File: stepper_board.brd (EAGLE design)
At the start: 100 x 80 mm, 77 parts, among them IC1 MCP1703DB, U2 MIC2005A-1YM5, Y1 12 MHz

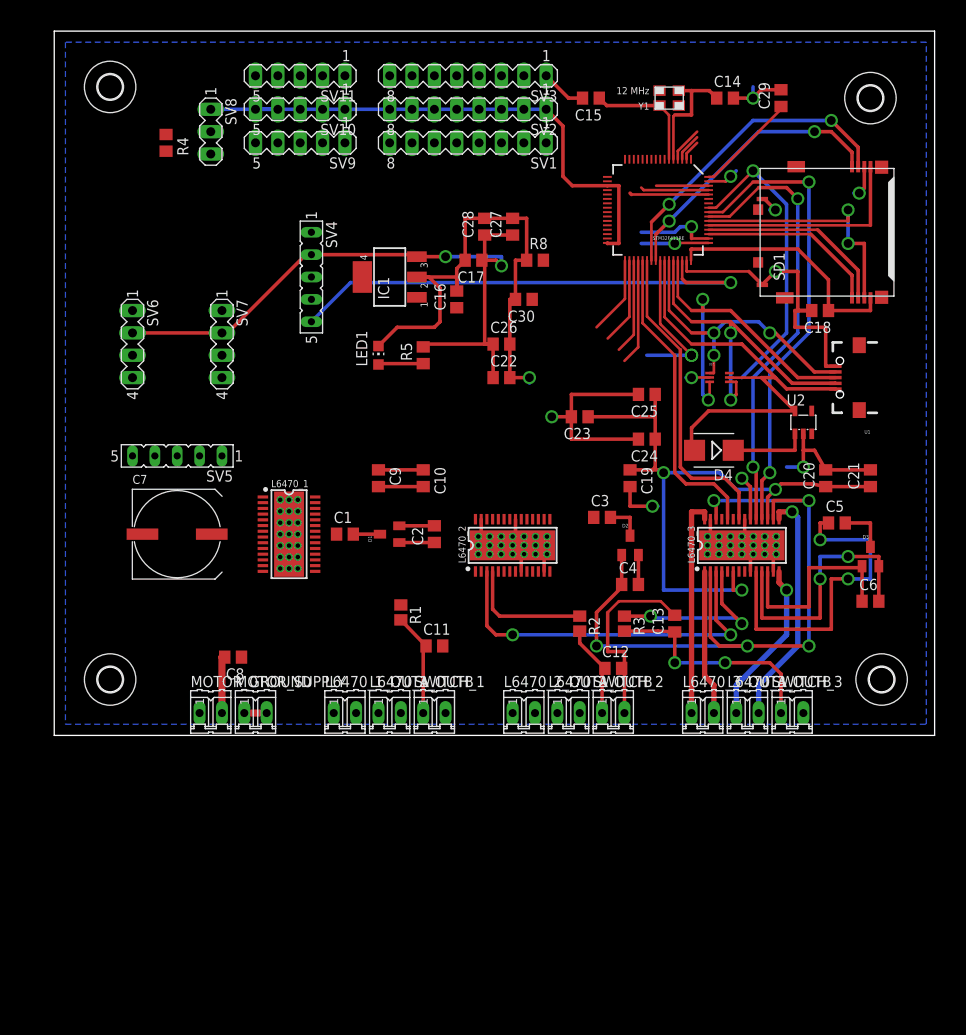
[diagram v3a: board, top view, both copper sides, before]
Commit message: Changed L6470 package footprint, added chip select pins to drivers, started routing
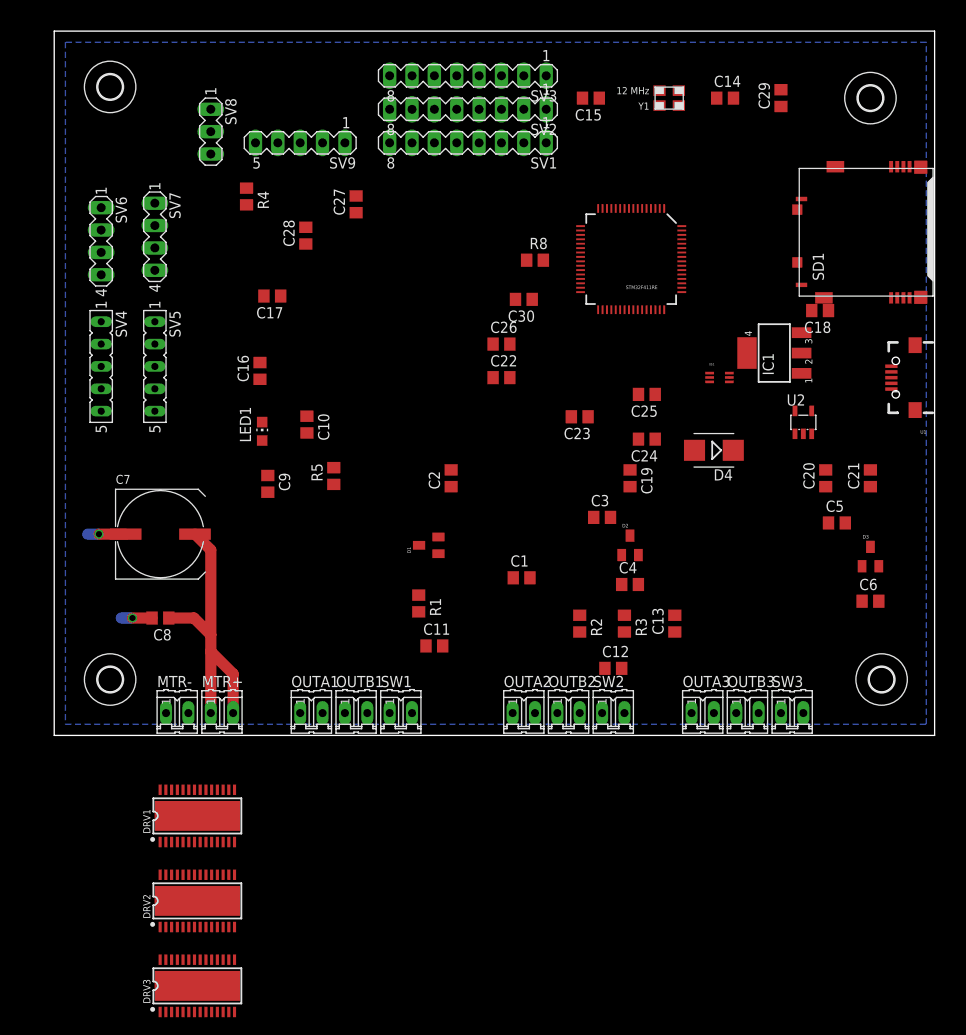
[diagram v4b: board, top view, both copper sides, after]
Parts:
- removed L6470_1, L6470_2, L6470_3: (no value), SparkFun-PowerIC:HTSSOP28
- removed L6470_1_OUTA, L6470_1_OUTB, MOTOR_GROUND, MOTOR_SUPPLY, SWITCH_1: (no value), con-amp-quick:02P
- removed SV10, SV11: (no value), con-lstb:MA05-1
- added DRV1, DRV2, DRV3: (no value), PowerIC_spark:HTSSOP28-NOPAD
- added MTR+, MTR-, OUTA1, OUTB1, SW1: (no value), con-amp-quick:02P
- moved IC1 44.5 mm to (81.8, 43.4)
- moved SV4 25.9 mm to (5.33, 41.9)
- moved C16 23.8 mm to (23.4, 41.4)
- moved C17 23.2 mm to (24.8, 49.9)
- moved C1 20.7 mm to (53.1, 17.9)
- moved C28 20.3 mm to (28.6, 56.8)
- moved C27 18.0 mm to (34.3, 60.3)
- moved R5 17.1 mm to (31.8, 29.5)
- moved LED1 15.8 mm to (23.6, 34.5)
- moved C10 14.5 mm to (28.7, 35.3)
- moved SV7 14.4 mm to (11.4, 56.6)
- moved C9 12.6 mm to (24.3, 28.6)
- moved SV6 12.2 mm to (5.33, 56.1)
- moved R4 11.0 mm to (21.8, 61.2)
- moved SV5 10.5 mm to (11.4, 41.9), turned to 270 degrees
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- renumbered L6470_2_OUTA to OUTA2, L6470_2_OUTB to OUTB2, L6470_3_OUTA to OUTA3, L6470_3_OUTB to OUTB3, SWITCH_2 to SW2, SWITCH_3 to SW3
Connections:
- removed net GPIO0: SV9.1
- removed net GPIO1: STM32F411RE.27, SV9.2
- new net CS1: DRV1.23
- new net CS2: DRV2.23, STM32F411RE.27
- new net CS3: DRV3.23
- new net OSCIN3: DRV3.7
- net +3V3: now also DRV1.17, DRV1.6, DRV2.17, DRV2.6, DRV3.17, DRV3.6, SV9.4; no longer L6470_1.17, L6470_1.6, L6470_2.17, L6470_2.6, L6470_3.17, L6470_3.6, SV10.1, SV10.2, SV10.3, SV10.4, SV10.5
- net 1_OUT1A: now also DRV1.1, OUTA1.2; no longer L6470_1.1, L6470_1_OUTA.1
- net 1_OUT1B: now also DRV1.14, OUTB1.1; no longer L6470_1.14, L6470_1_OUTB.1
- net 1_OUT2A: now also DRV1.28, OUTA1.1; no longer L6470_1.28, L6470_1_OUTA.2
- net 1_OUT2B: now also DRV1.15, OUTB1.2; no longer L6470_1.15, L6470_1_OUTB.2
- net 2_OUT1A: now also DRV2.1, OUTA2.2; no longer L6470_2.1, OUTA2.1
- net 2_OUT1B: now also DRV2.14; no longer L6470_2.14
- net 2_OUT2A: now also DRV2.28, OUTA2.1; no longer L6470_2.28, OUTA2.2
- net 2_OUT2B: now also DRV2.15; no longer L6470_2.15
- net 3_OUT1A: now also DRV3.1; no longer L6470_3.1
- net 3_OUT1B: now also DRV3.14; no longer L6470_3.14
- net 3_OUT2A: now also DRV3.28; no longer L6470_3.28
- net 3_OUT2B: now also DRV3.15; no longer L6470_3.15
- net BUSY1: now also DRV1.22; no longer L6470_1.22
- net BUSY2: now also DRV2.22; no longer L6470_2.22
- net BUSY3: now also DRV3.22; no longer L6470_3.22
- net FLAG1: now also DRV1.24; no longer L6470_1.24
- net FLAG2: now also DRV2.24; no longer L6470_2.24
- net FLAG3: now also DRV3.24; no longer L6470_3.24
- net GND: now also DRV1.13, DRV1.21, DRV1.27, DRV1.9, DRV1.GND, DRV2.13, DRV2.21, DRV2.27, DRV2.9, DRV2.GND, DRV3.13, DRV3.21, DRV3.27, DRV3.9, DRV3.GND, MTR-.1, MTR-.2, SV9.5, SW1.2; no longer L6470_1.13, L6470_1.21, L6470_1.27, L6470_1.9, L6470_1.GND@PAD, L6470_2.13, L6470_2.21, L6470_2.27, L6470_2.9, L6470_2.GND@PAD, L6470_3.13, L6470_3.21, L6470_3.27, L6470_3.9, L6470_3.GND@PAD, MOTOR_GROUND.1, MOTOR_GROUND.2, SV11.1, SV11.2, SV11.3, SV11.4, SV11.5, SWITCH_1.2
- net GPIO2: now also SV9.1; no longer SV9.3
- net GPIO3: now also SV9.2; no longer SV9.4
- net GPIO4: now also SV9.3; no longer SV9.5
- net N$1: now also DRV1.10; no longer L6470_1.10
- net N$10: now also DRV3.11; no longer L6470_3.11
- net N$11: now also SW1.1; no longer SWITCH_1.1
- net N$12: now also DRV2.4; no longer L6470_2.4
- net N$14: now also DRV3.4; no longer L6470_3.4
- net N$3: now also DRV1.11; no longer L6470_1.11
- net N$4: now also DRV2.10; no longer L6470_2.10
- net N$6: now also DRV2.11; no longer L6470_2.11
- net N$7: now also DRV1.4; no longer L6470_1.4
- net N$8: now also DRV3.10; no longer L6470_3.10
- net OSCIN1: now also DRV1.7; no longer L6470_1.7
- net OSCIN2: now also DRV2.7; no longer L6470_2.7
- net OSCOUT1: now also DRV1.8; no longer L6470_1.8
- net OSCOUT2: now also DRV2.8; no longer L6470_2.8
- net OSCOUT3: now also DRV3.8; no longer L6470_3.8
- net RESET: now also DRV1.3, DRV2.3, DRV3.3; no longer L6470_2.3, L6470_3.3
- net SPI1_MISO: now also DRV1.18, DRV2.18, DRV3.18; no longer L6470_1.18, L6470_2.18, L6470_3.18
- net SPI1_MOSI: now also DRV1.20, DRV2.20, DRV3.20; no longer L6470_1.20, L6470_2.20, L6470_3.20
- net SPI1_SCK: now also DRV1.19, DRV2.19, DRV3.19; no longer L6470_1.19, L6470_2.19, L6470_3.19
- net STCK1: now also DRV1.25; no longer L6470_1.25
- net STCK2: now also DRV2.25; no longer L6470_2.25
- net STCK3: now also DRV3.25; no longer L6470_3.25
- net VCC: now also DRV1.12, DRV1.16, DRV1.2, DRV1.26, DRV2.12, DRV2.16, DRV2.2, DRV2.26, DRV3.12, DRV3.16, DRV3.2, DRV3.26, MTR+.1, MTR+.2; no longer L6470_1.12, L6470_1.16, L6470_1.2, L6470_1.26, L6470_2.12, L6470_2.16, L6470_2.2, L6470_2.26, L6470_3.12, L6470_3.16, L6470_3.2, L6470_3.26, MOTOR_SUPPLY.1, MOTOR_SUPPLY.2
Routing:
- net +3V3: track 260.3 -> 0.00 mm, vias 5 -> 0
- net GND: track 236.7 -> 7.80 mm, vias 10 -> 2
- net VCC: track 113.9 -> 34.7 mm, vias 5 -> 0
- net JSSW: track 57.2 -> 0.00 mm, vias 1 -> 0
- net USB_VBUS: track 55.1 -> 0.02 mm
- net SPI1_MISO: track 53.3 -> 0.00 mm, vias 2 -> 0
- net SPI1_SCK: track 50.7 -> 0.00 mm, vias 2 -> 0
- net RESET: track 42.2 -> 0.00 mm, vias 2 -> 0
- net USB_DP: track 40.9 -> 0.00 mm, vias 2 -> 0
- net USB_DM: track 39.1 -> 0.00 mm, vias 2 -> 0
- net SPI1_MOSI: track 39.0 -> 0.00 mm, vias 2 -> 0
- net N$8: track 38.3 -> 0.00 mm, vias 2 -> 0
- net SD_D0: track 36.1 -> 0.00 mm, vias 2 -> 0
- net BUSY3: track 35.9 -> 0.00 mm
- net FLAG3: track 35.2 -> 0.00 mm
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
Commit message: Routed tons o' stuff
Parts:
- removed D4: ES2D, diode:SMB
- removed LED1: (no value), led:CHIP-LED0805
- added D5: PD3S160, diode:POWERDI323
- added PWR: (no value), led:CHIP-LED0805
- added SV10: (no value), con-lstb:MA05-1
- SV9: device con-lstb:MA05-1 -> con-lstb:MA04-1
- moved C29 96.3 mm to (16.0, 2.74), turned to 270 degrees
- moved U1 96.2 mm to (1.78, 47.2), turned to 0 degrees
- moved DRV1 94.8 mm to (76.2, 64.3), turned to 90 degrees
- moved OUTB1 90.3 mm to (97.5, 67.1), turned to 90 degrees
- moved OUTA1 90.1 mm to (97.5, 61.2), turned to 90 degrees
- moved SD1 88.6 mm to (29.7, 1.14), turned to 0 degrees
- moved DRV2 86.6 mm to (76.5, 43.4), turned to 90 degrees
- moved DRV3 78.0 mm to (77.0, 20.6), turned to 90 degrees
- moved SW1 77.9 mm to (97.5, 54.4), turned to 90 degrees
- moved MTR- 68.6 mm to (82.5, 2.54)
- moved U2 68.5 mm to (18.3, 50.8)
- moved U$1 66.7 mm to (9.14, 47.2), flipped to the bottom, turned to 90 degrees
- moved IC1 63.3 mm to (20.3, 58.4), turned to 0 degrees
- moved D1 61.7 mm to (87.9, 63.4), turned to 180 degrees
- moved OUTB2 58.6 mm to (97.8, 46.0), turned to 90 degrees
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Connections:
- removed net GPIO3: STM32F411RE.50, SV9.2
- removed net GPIO4: STM32F411RE.41, SV9.3
- removed net OSCIN1: DRV1.7
- removed net OSCIN2: DRV2.7
- removed net OSCIN3: DRV3.7
- removed net OSCOUT1: DRV1.8
- removed net OSCOUT2: DRV2.8
- removed net OSCOUT3: DRV3.8
- new net GPIO1: STM32F411RE.49, SV9.3
- new net SPI2_MISO: SV10.3
- new net USB_EN: STM32F411RE.41, U2.3
- net +3V3: now also STM32F411RE.1, SV10.2, SV9.2; no longer SV9.4
- net GND: now also DRV1.5, DRV2.5, DRV3.5, PWR.C, SV10.1, SV9.1; no longer LED1.C, SV9.5
- net GPIO2: now also STM32F411RE.50, SV9.4; no longer STM32F411RE.49, SV9.1
- net N$20: now also PWR.A; no longer LED1.A
- net SPI2_MOSI: now also SV10.4
- net SPI2_SCK: now also SV10.5
- net USB_VBUS: now also D5.A; no longer D4.A
- net V+: now also D5.C; no longer D4.C
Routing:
- net +3V3: track 0.00 -> 118.6 mm, vias 0 -> 9
- net VCC: track 34.7 -> 151.2 mm
- net SD_D0: track 0.00 -> 62.5 mm, vias 0 -> 2
- net SD_D1: track 0.00 -> 57.5 mm, vias 0 -> 2
- net SD_CMD: track 0.00 -> 54.1 mm, vias 0 -> 2
- net USB_VBUS: track 0.02 -> 48.0 mm, vias 0 -> 1
- net SD_D3: track 0.00 -> 47.4 mm
- net SD_D2: track 0.00 -> 47.1 mm, vias 0 -> 2
- net GND: track 7.80 -> 53.8 mm, vias 2 -> 19
- net SD_CLK: track 0.00 -> 42.8 mm, vias 0 -> 2
- net USB_ID: track 0.00 -> 35.1 mm, vias 0 -> 3
- net USB_DM: track 0.00 -> 34.5 mm, vias 0 -> 1
- net USB_DP: track 0.00 -> 33.9 mm, vias 0 -> 1
- net 1_OUT2B: track 0.00 -> 32.5 mm
- net 2_OUT2B: track 0.00 -> 32.0 mm
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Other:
- board size 100 x 80 mm -> 101.1 x 81.3 mm

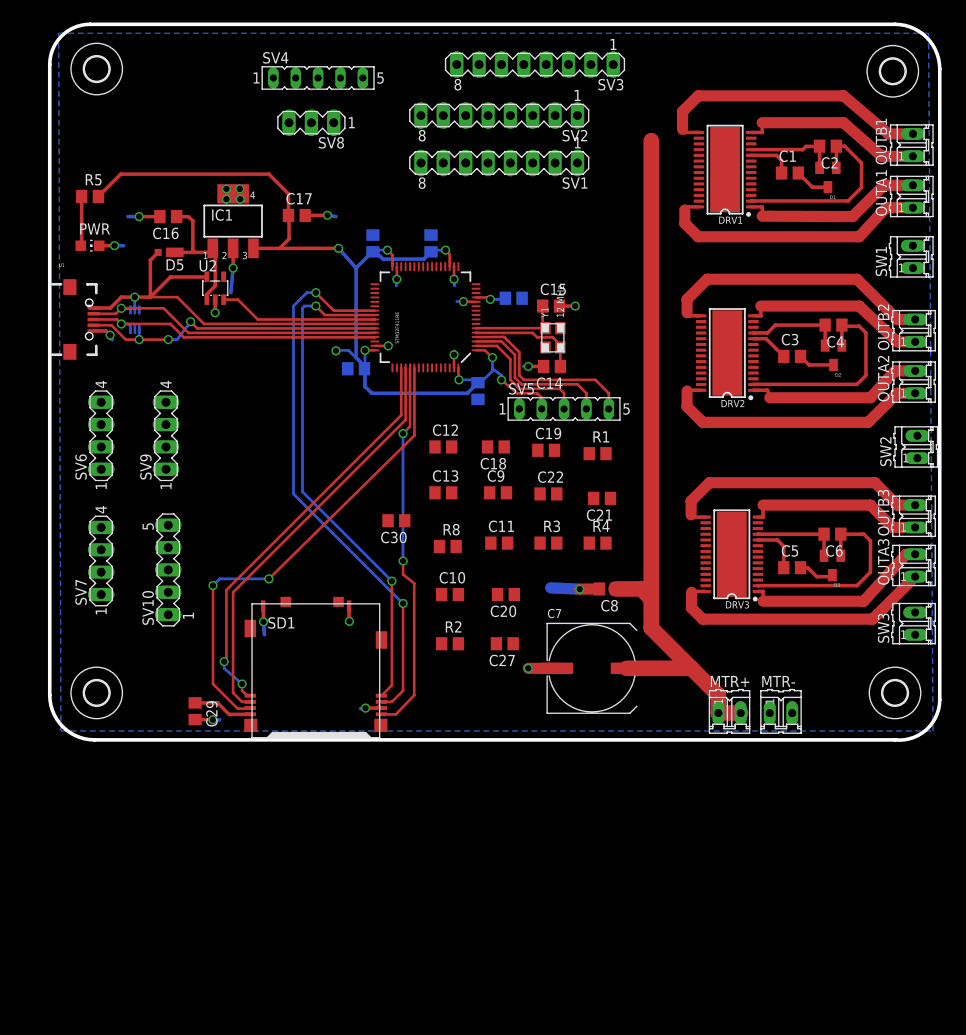
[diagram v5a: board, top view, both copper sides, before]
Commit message: Finished routing! Also added test points.
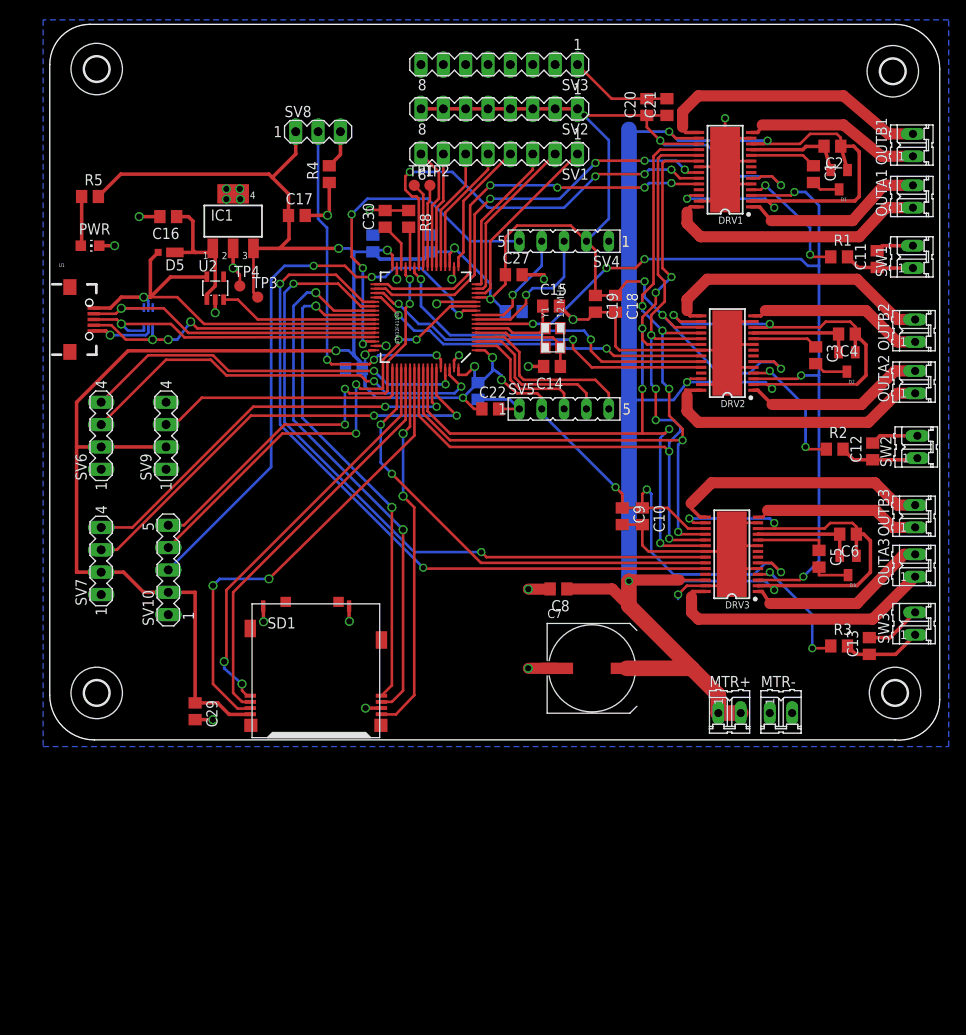
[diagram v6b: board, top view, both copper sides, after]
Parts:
- added TP1, TP2, TP3, TP4: PTR1B1,27, testpad:B1,27
- moved C20 57.6 mm to (67.3, 71.4), turned to 90 degrees
- moved C11 53.7 mm to (93.5, 54.1), turned to 90 degrees
- moved R4 51.8 mm to (31.2, 63.8), turned to 90 degrees
- moved C13 51.4 mm to (92.6, 10.2), turned to 90 degrees
- moved R2 49.0 mm to (88.6, 32.5)
- moved C12 48.8 mm to (93.0, 32.3), turned to 90 degrees
- moved C21 45.1 mm to (69.6, 71.4), turned to 90 degrees
- moved C27 41.9 mm to (52.2, 52.3), turned to 0 degrees
- moved R8 37.5 mm to (40.3, 58.7), turned to 270 degrees
- moved R1 35.4 mm to (89.2, 54.4)
- moved R3 35.0 mm to (89.2, 10.2)
- moved C30 34.3 mm to (37.6, 58.7), turned to 90 degrees
- moved SV4 33.5 mm to (57.9, 56.1), turned to 180 degrees
- moved C10 23.6 mm to (66.8, 24.9), turned to 270 degrees
- moved C18 21.2 mm to (63.8, 49.0), turned to 270 degrees
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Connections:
- removed net GPIO2: STM32F411RE.50, SV9.4
- net +3V3: now also TP3.TP
- net ADC0: now also STM32F411RE.14
- net ADC1_14: now also TP2.TP
- net ADC1_15: now also TP1.TP
- net ADC6: now also STM32F411RE.22
- net CS1: now also STM32F411RE.26
- net CS3: now also STM32F411RE.50
- net GND: now also SV9.4, TP4.TP
- net SPI2_MISO: now also STM32F411RE.10
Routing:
- net +3V3: track 118.6 -> 426.5 mm, vias 9 -> 19
- net VCC: track 151.2 -> 303.9 mm, vias 0 -> 12
- net GND: track 53.8 -> 201.3 mm, vias 19 -> 23
- net RESET: track 0.00 -> 106.6 mm, vias 0 -> 6
- net SPI1_SCK: track 0.00 -> 97.6 mm, vias 0 -> 5
- net SPI1_MOSI: track 0.00 -> 97.2 mm, vias 0 -> 6
- net SPI1_MISO: track 0.00 -> 94.4 mm, vias 0 -> 5
- net FLAG3: track 0.00 -> 83.6 mm, vias 0 -> 2
- net BUSY3: track 0.00 -> 80.6 mm, vias 0 -> 2
- net SPI2_MISO: track 0.00 -> 65.7 mm, vias 0 -> 3
- net CS3: track 0.00 -> 53.1 mm, vias 0 -> 2
- net USART1_RX: track 0.00 -> 53.1 mm, vias 0 -> 2
- net SPI2_MOSI: track 0.00 -> 52.2 mm, vias 0 -> 4
- net SPI2_SCK: track 0.00 -> 49.4 mm, vias 0 -> 4
- net CS1: track 0.00 -> 48.6 mm, vias 0 -> 4
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
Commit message: Added reset switch, thermal pad vias, cleaned up some traces, and fixed usb footprint
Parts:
- added C31: 100n, rcl:C0805
- added R6: 4k7, rcl:R0805
- added S1: (no value), switch-omron:B3F-10XX
- moved C10 4.35 mm to (62.5, 25.4)
- moved C9 4.35 mm to (60.2, 25.4)
- moved C12 0.76 mm to (92.2, 32.3)
- moved C18 0.76 mm to (63.0, 49.0)
- moved D1 0.76 mm to (88.4, 63.1)
- moved C1 0.51 mm to (85.7, 63.8)
- moved C19 0.51 mm to (61.0, 49.0)
- moved OUTA1 0.25 mm to (97.8, 61.2)
- moved OUTB1 0.25 mm to (97.8, 67.1)
- moved SW1 0.25 mm to (97.8, 54.4)
- moved MTR+ 0.25 mm to (76.7, 2.29)
- moved MTR- 0.25 mm to (82.5, 2.29)
- moved R3 0.25 mm to (88.9, 10.2)
- moved SW2 0.25 mm to (97.8, 32.8)
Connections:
- net +3V3: now also R6.2
- net GND: now also C31.2, S1.4
- net RESET: now also C31.1, R6.1, S1.1
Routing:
- net RESET: track 106.6 -> 167.0 mm, vias 6 -> 7
- net +3V3: track 426.5 -> 449.9 mm, vias 19 -> 21
- net GND: track 201.3 -> 212.7 mm, vias 23 -> 57
- net VCC: track 303.9 -> 302.7 mm
- net SPI1_SCK: track 97.6 -> 96.7 mm
- net SPI1_MOSI: track 97.2 -> 96.4 mm
- net N$1: track 7.55 -> 7.05 mm
- added copper zone on layer 1, net GND
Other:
- board text added: "Telescope Stepper Driver v1 John Barry Anthony Lombardi ME 507 Fall 2016"
